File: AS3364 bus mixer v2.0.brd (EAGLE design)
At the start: 44.5 x 32.4 mm, 65 parts, among them IC1 TL072JT, IC2 TL072JT, IC3 TL072JT, IC30 TL072JT, IC4 TL072JT, IC5 79L09F, IC6 78L09F, IC7 CH446Q

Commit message: Working on v2.0
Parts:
- added R37, R38, R39, R40, R41, R42, R43, R44: 36k, rcl:R0402
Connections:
- net SW1 renamed SW1A
- removed net BITCRUSH_IN: IC7.15, SV1.13
- removed net DIST_IN: IC7.17, SV1.14
- removed net SW2: IC7.30, R15.2
- removed net SW3: IC7.29, R17.2
- removed net SW4: IC7.28, R14.2
- removed net SW5: IC7.27, R33.2
- removed net SW6: IC7.26, R32.2
- removed net SW7: IC7.3, R34.2
- removed net SW8: IC7.4, R31.2
- new net SW1B: IC7.30, R40.2
- new net SW2A: IC7.29, R15.2
- new net SW2B: IC7.28, R37.2
- new net SW3A: IC7.27, R17.2
- new net SW3B: IC7.26
- new net SW4A: IC7.3, R14.2
- new net SW4B: IC7.4, R38.2, R39.2
- new net SW5A: IC7.5, R33.2
- new net SW5B: IC7.6, R44.2
- new net SW6A: IC7.7, R32.2
- new net SW6B: IC7.8, R41.2
- new net SW7A: IC7.25, R34.2
- new net SW7B: IC7.24, R43.2
- new net SW8A: IC7.1, R31.2
- new net SW8B: IC7.2, R42.2
- net OUT1: now also R40.1
- net OUT2: now also R37.1
- net OUT3: now also R39.1
- net OUT4: now also R38.1
- net OUT5: now also R44.1
- net OUT6: now also R41.1
- net OUT7: now also R43.1
- net OUT8: now also R42.1
- net SUM_A: no longer IC7.5
- net SUM_B: no longer IC7.6
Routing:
- net DIST_IN: track 31.5 -> 0.00 mm, vias 1 -> 0
- net SW8: track 30.9 -> 0.00 mm, vias 2 -> 0
- net SW8A: track 0.00 -> 30.9 mm, vias 0 -> 2
- net SW7: track 30.7 -> 0.00 mm, vias 4 -> 0
- net SW7A: track 0.00 -> 29.4 mm, vias 0 -> 4
- net BITCRUSH_IN: track 25.4 -> 0.00 mm, vias 1 -> 0
- net SW5: track 23.4 -> 0.00 mm, vias 2 -> 0
- net SW3: track 22.7 -> 0.00 mm, vias 2 -> 0
- net SW5A: track 0.00 -> 20.8 mm, vias 0 -> 2
- net SW3A: track 0.00 -> 20.4 mm, vias 0 -> 2
- net SW2: track 17.0 -> 0.00 mm, vias 2 -> 0
- net SW6: track 16.7 -> 0.00 mm, vias 2 -> 0
- net SW6A: track 0.00 -> 16.7 mm, vias 0 -> 2
- net SW2A: track 0.00 -> 15.9 mm, vias 0 -> 2
- net SW4: track 14.2 -> 0.00 mm, vias 2 -> 0
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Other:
- board text added: "Pre-filter bus mixer v2.0"
- board text removed: "Pre-filter bus mixer v1.0"

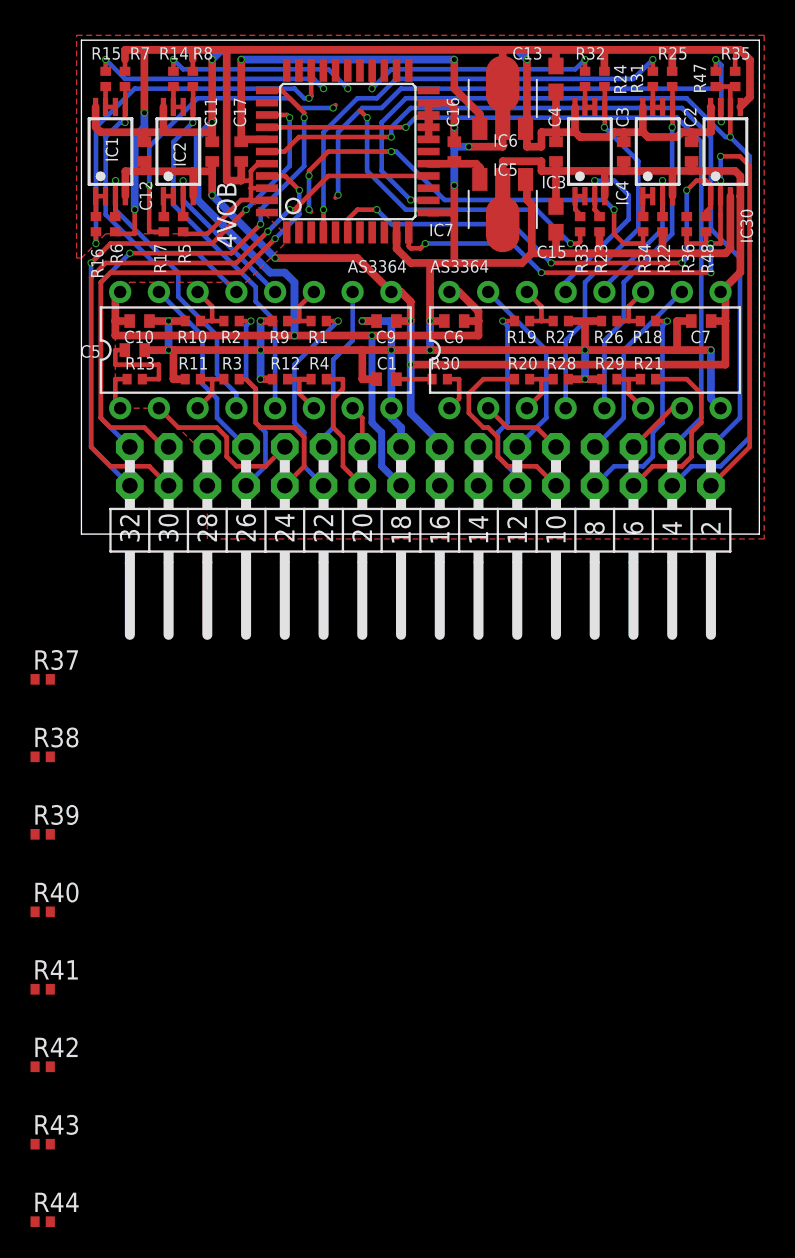
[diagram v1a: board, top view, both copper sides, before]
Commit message: Traced new lines for bus mixer v2.0, missing lines under CH446Q
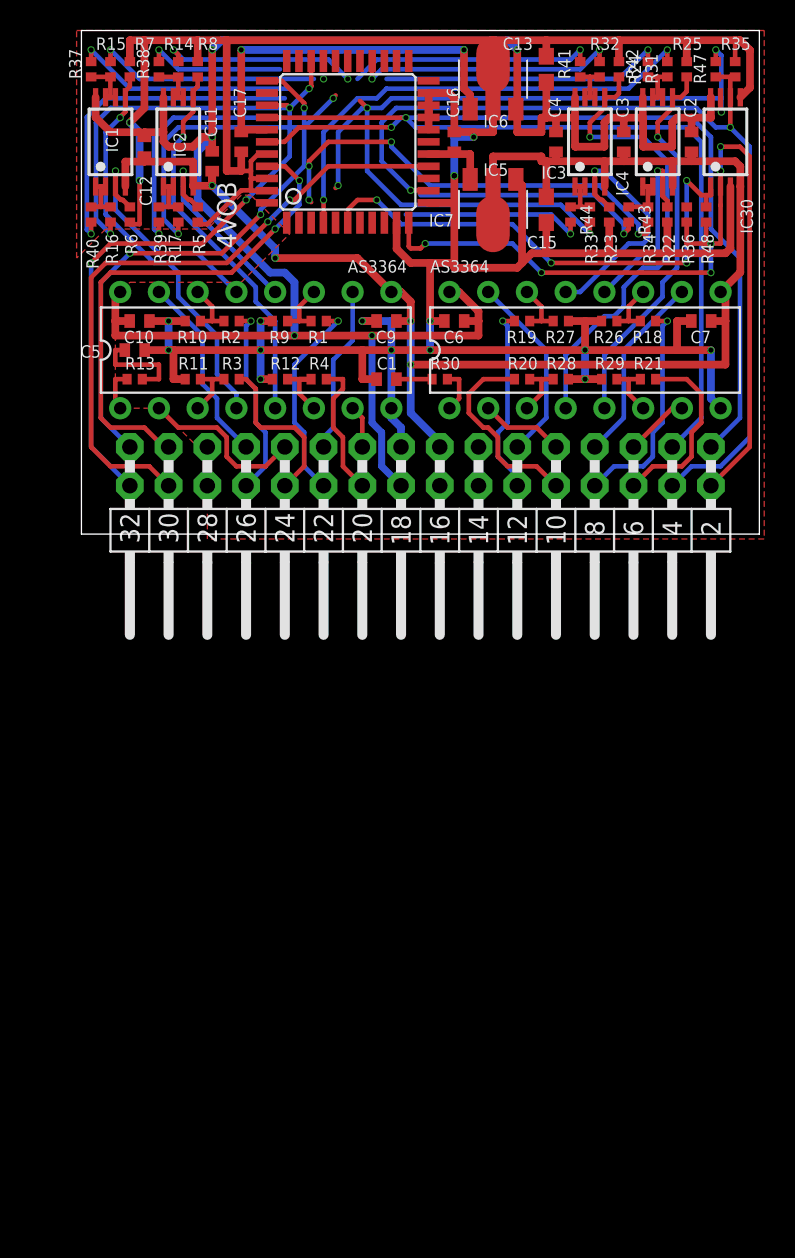
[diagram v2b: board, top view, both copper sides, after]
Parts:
- moved R42 76.5 mm to (37.1, 30.8), turned to 90 degrees
- moved R44 74.6 mm to (32.1, 21.3), turned to 270 degrees
- moved R43 72.1 mm to (35.9, 21.3), turned to 270 degrees
- moved R41 69.9 mm to (32.7, 30.8), turned to 90 degrees
- moved R40 45.8 mm to (0.64, 21.3), turned to 270 degrees
- moved R38 45.7 mm to (5.08, 30.8), turned to 90 degrees
- moved R39 41.3 mm to (5.08, 21.3), turned to 270 degrees
- moved R37 40.1 mm to (0.64, 30.8), turned to 90 degrees
- moved IC6 1.42 mm to (27.0, 30.2)
- moved R16 1.14 mm to (1.91, 21.3)
- moved R17 1.14 mm to (6.35, 21.3)
- moved R5 1.14 mm to (7.62, 21.3)
- moved R6 1.14 mm to (3.17, 21.3)
- moved R24 1.14 mm to (35.2, 30.8)
- moved R25 1.14 mm to (39.7, 30.8)
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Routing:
- net SW4B: track 0.00 -> 24.9 mm, vias 0 -> 2
- net SW1B: track 0.00 -> 22.0 mm, vias 0 -> 1
- net SW8B: track 0.00 -> 18.7 mm, vias 0 -> 1
- net SW6B: track 0.00 -> 16.2 mm, vias 0 -> 1
- net SW7B: track 0.00 -> 15.7 mm, vias 0 -> 1
- net SW2B: track 0.00 -> 14.8 mm, vias 0 -> 1
- net SW5B: track 0.00 -> 12.1 mm, vias 0 -> 1
- net +12V: track 128.9 -> 135.7 mm
- net CON6: track 24.0 -> 30.8 mm
- net BUS_B: track 57.3 -> 60.4 mm
- net GND: track 237.5 -> 240.3 mm
- net CON5: track 13.2 -> 15.9 mm
- net CON8: track 22.9 -> 25.3 mm
- net OUT4: track 1.99 -> 3.58 mm
- net OUT2: track 1.99 -> 3.57 mm
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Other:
- board size 44.5 x 32.4 mm -> 44.5 x 33 mm

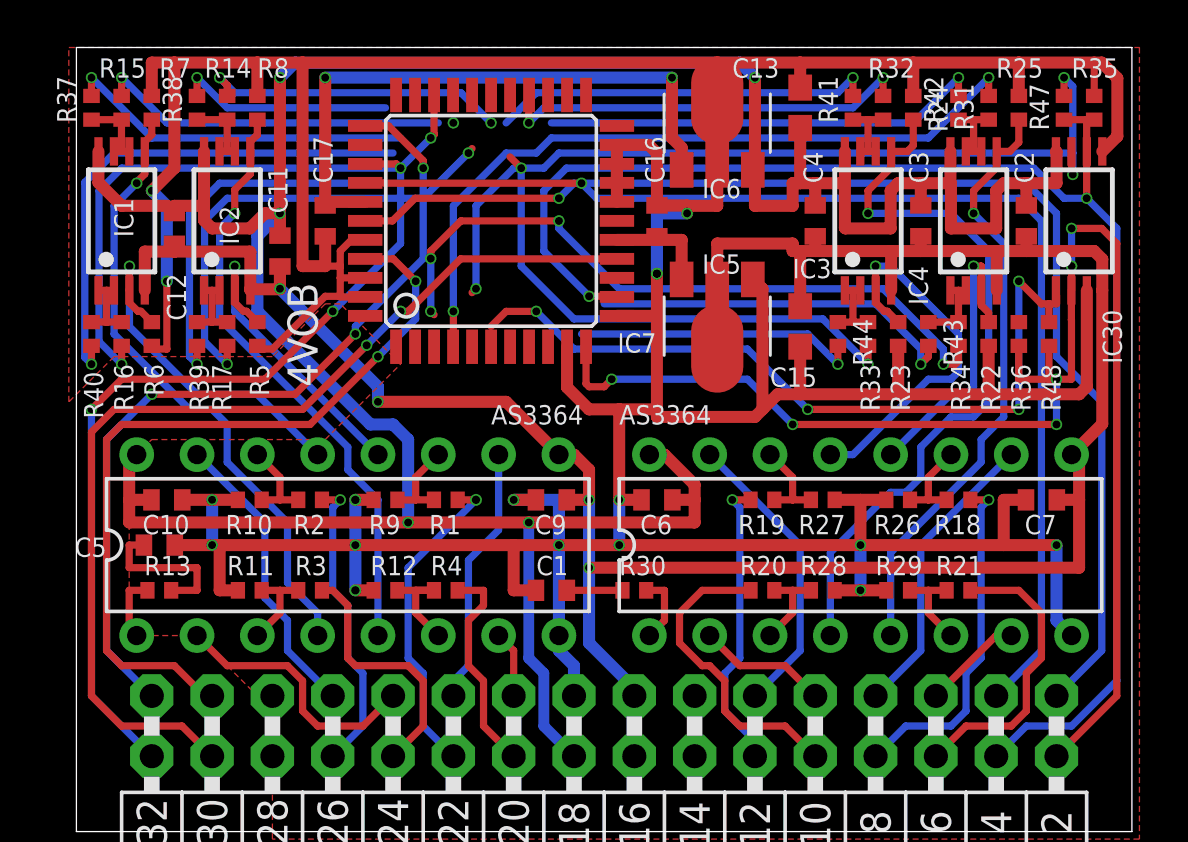
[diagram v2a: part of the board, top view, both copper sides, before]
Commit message: Finished tracing v2.0 of bus mixer
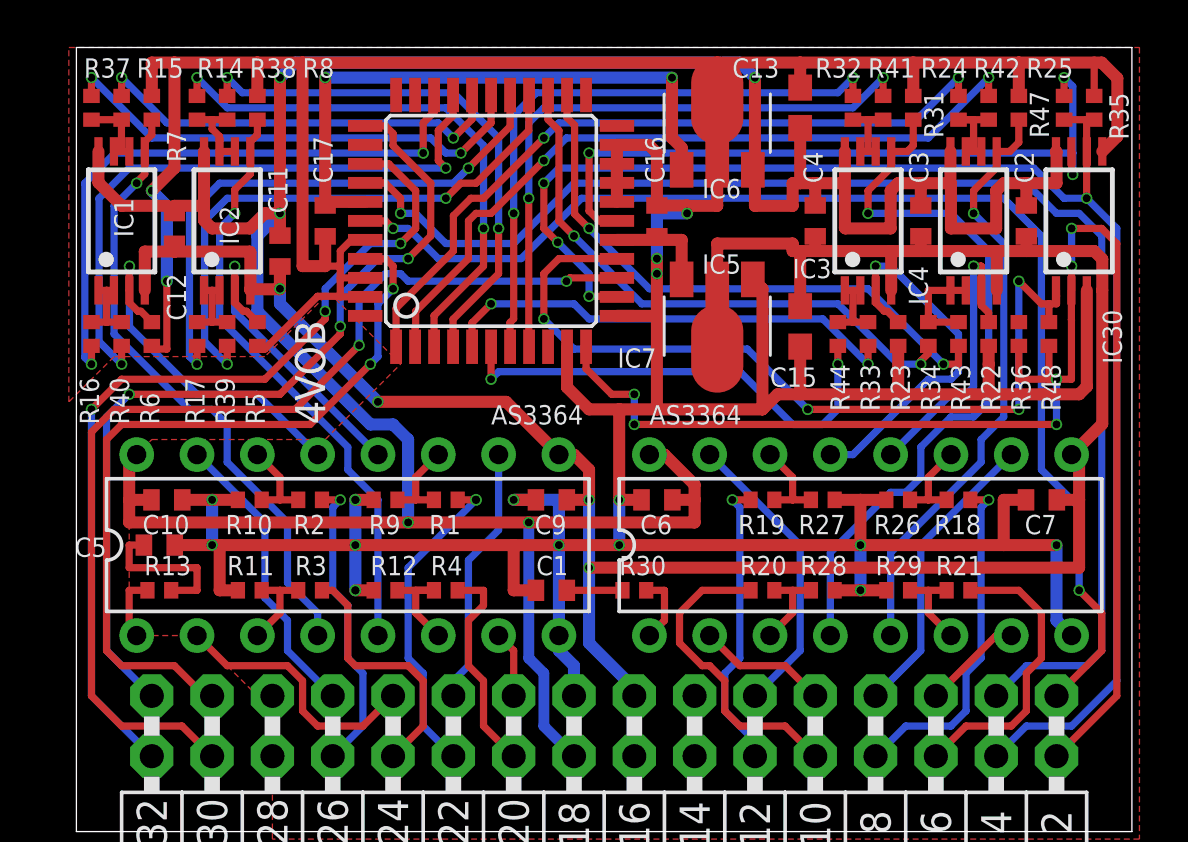
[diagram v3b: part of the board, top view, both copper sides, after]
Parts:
- moved R34 1.27 mm to (35.9, 21.3)
- moved R43 1.27 mm to (37.1, 21.3)
- moved R16 1.27 mm to (0.64, 21.3)
- moved R40 1.27 mm to (1.91, 21.3)
- moved R14 1.27 mm to (5.08, 30.8)
- moved R17 1.27 mm to (5.08, 21.3)
- moved R38 1.27 mm to (6.35, 30.8)
- moved R39 1.27 mm to (6.35, 21.3)
- moved R31 1.27 mm to (37.1, 30.8)
- moved R32 1.27 mm to (32.7, 30.8)
- moved R41 1.27 mm to (34.0, 30.8)
- moved R42 1.27 mm to (38.4, 30.8)
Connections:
- net SUM_A: now also IC7.17
- net SUM_B: now also IC7.15
- net SW3B: now also R39.2
- net SW4B: no longer R39.2
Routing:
- net SW3B: track 0.00 -> 23.9 mm, vias 0 -> 2
- net SW8B: track 18.7 -> 31.4 mm, vias 1 -> 2
- net SW4A: track 13.1 -> 23.4 mm
- net SW6B: track 16.2 -> 25.9 mm, vias 1 -> 2
- net SW7B: track 15.7 -> 24.7 mm, vias 1 -> 2
- net SW6A: track 17.6 -> 25.5 mm
- net SW5B: track 12.1 -> 20.0 mm, vias 1 -> 2
- net FX_A: track 49.9 -> 57.1 mm
- net SW2B: track 14.8 -> 20.6 mm, vias 1 -> 2
- net SUM_A: track 35.9 -> 30.2 mm
- net SW7A: track 29.2 -> 24.1 mm, vias 4 -> 2
- net SW1B: track 22.0 -> 26.7 mm, vias 1 -> 2
- net SW3A: track 19.7 -> 23.6 mm
- net SW2A: track 14.9 -> 17.9 mm
- net SUM_B: track 32.7 -> 35.6 mm
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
